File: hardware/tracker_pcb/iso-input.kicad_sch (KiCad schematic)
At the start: 5 parts, among them Q1 LTV-817S-TA1-D

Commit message: Including LORA wio-sx1262
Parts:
- D4: symbol ESP32-C6-EVB_Rev_A:D_Small -> Device:D_Filled; LCSC (none) -> C81598
- LED1: symbol ESP32-C6-EVB_Rev_A:LED -> Device:LED; LCSC (none) -> C2288
- Q1: LCSC (none) -> C114603
- R13: renamed from R11; LCSC (none) -> C22967
- renumbered R10 to R12
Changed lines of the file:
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@@
+	(wire
+		(pts
+			(xy 139.7 85.09) (xy 146.05 85.09)
+		)
+		(stroke
+			(width 0)
+			(type default)
+		)
+	)
 	(wire
 		(pts
@@
 	(wire
 		(pts
-			(xy 130.81 85.09) (xy 127 85.09)
-		)
-		(stroke
-			(width 0)
-			(type default)
-		)
-	)
-	(wire
-		(pts
 			(xy 173.99 90.17) (xy 173.99 97.79)
 		)
@@
 	(wire
 		(pts
-			(xy 140.97 85.09) (xy 146.05 85.09)
-		)
-		(stroke
-			(width 0)
-			(type default)
-		)
-	)
-	(wire
-		(pts
-			(xy 127 88.9) (xy 127 85.09)
+			(xy 127 85.09) (xy 132.08 85.09)
 		)
 		(stroke
@@
 	(wire
 		(pts
+			(xy 127 95.25) (xy 127 97.79)
+		)
+		(stroke
+			(width 0)
+			(type default)
+		)
+	)
+	(wire
+		(pts
 			(xy 127 97.79) (xy 146.05 97.79)
 		)
@@
 	(wire
 		(pts
-			(xy 127 93.98) (xy 127 97.79)
+			(xy 127 85.09) (xy 127 87.63)
 		)
 		(stroke
@@
 	)
 	(symbol
-		(lib_id "ESP32-C6-EVB_Rev_A:LED")
+		(lib_id "Device:LED")
 		(at 135.89 85.09 180)
 		(unit 1)
@@
 			(effects
 				(font
-					(size 1.524 1.524)
-				)
-				(hide yes)
-			)
-		)
-		(property "Datasheet" ""
+					(size 1.27 1.27)
+				)
+				(hide yes)
+			)
+		)
+		(property "Datasheet" "~"
 			(at 135.89 85.09 0)
 			(effects
 				(font
-					(size 1.524 1.524)
-				)
-			)
-		)
-		(property "Description" ""
+					(size 1.27 1.27)
+				)
+				(hide yes)
+			)
+		)
+		(property "Description" "Light emitting diode"
 			(at 135.89 85.09 0)
 			(effects
@@
 					(size 1.27 1.27)
 				)
+				(hide yes)
 			)
 		)
@@
 				(font
 					(size 1.524 1.524)
+				)
+				(hide yes)
+			)
+		)
+		(property "Sim.Pins" "1=K 2=A"
+			(at 135.89 85.09 0)
+			(effects
+				(font
+					(size 1.27 1.27)
+				)
+				(hide yes)
+			)
+		)
+		(property "LCSC" "C2288"
+			(at 133.35 82.55 0)
+			(effects
+				(font
+					(size 1.27 1.27)
 				)
 				(hide yes)
@@
 		(dnp no)
 		(fields_autoplaced yes)
-		(property "Reference" "R10"
+		(property "Reference" "R12"
 			(at 106.68 78.74 90)
 			(effects
@@
 			(project "tracker_pcb"
 				(path "/6aaa9514-f94e-4843-90d0-16960e4e49cb/04328898-976a-48a2-86bf-9938cb4aefd5"
+					(reference "R14")
+					(unit 1)
+				)
+				(path "/6aaa9514-f94e-4843-90d0-16960e4e49cb/45a2292e-2f51-4a4c-a627-74180fb6fdfe"
+					(reference "R18")
+					(unit 1)
+				)
+				(path "/6aaa9514-f94e-4843-90d0-16960e4e49cb/45c78875-26ba-4b22-bc82-79a51b704824"
 					(reference "R12")
 					(unit 1)
 				)
-				(path "/6aaa9514-f94e-4843-90d0-16960e4e49cb/45a2292e-2f51-4a4c-a627-74180fb6fdfe"
+				(path "/6aaa9514-f94e-4843-90d0-16960e4e49cb/b128d80c-4aa3-4c05-bd4f-543db8edd72e"
 					(reference "R16")
-					(unit 1)
-				)
-				(path "/6aaa9514-f94e-4843-90d0-16960e4e49cb/45c78875-26ba-4b22-bc82-79a51b704824"
-					(reference "R10")
-					(unit 1)
-				)
-				(path "/6aaa9514-f94e-4843-90d0-16960e4e49cb/b128d80c-4aa3-4c05-bd4f-543db8edd72e"
-					(reference "R14")
 					(unit 1)
 				)
@@
 		(on_board yes)
 		(dnp no)
-		(property "Reference" "#PWR015"
+		(property "Reference" "#PWR016"
 			(at 173.99 104.14 0)
 			(effects
@@
 			(project "tracker_pcb"
 				(path "/6aaa9514-f94e-4843-90d0-16960e4e49cb/04328898-976a-48a2-86bf-9938cb4aefd5"
+					(reference "#PWR017")
+					(unit 1)
+				)
+				(path "/6aaa9514-f94e-4843-90d0-16960e4e49cb/45a2292e-2f51-4a4c-a627-74180fb6fdfe"
+					(reference "#PWR019")
+					(unit 1)
+				)
+				(path "/6aaa9514-f94e-4843-90d0-16960e4e49cb/45c78875-26ba-4b22-bc82-79a51b704824"
 					(reference "#PWR016")
 					(unit 1)
 				)
-				(path "/6aaa9514-f94e-4843-90d0-16960e4e49cb/45a2292e-2f51-4a4c-a627-74180fb6fdfe"
+				(path "/6aaa9514-f94e-4843-90d0-16960e4e49cb/b128d80c-4aa3-4c05-bd4f-543db8edd72e"
 					(reference "#PWR018")
-					(unit 1)
-				)
-				(path "/6aaa9514-f94e-4843-90d0-16960e4e49cb/45c78875-26ba-4b22-bc82-79a51b704824"
-					(reference "#PWR015")
-					(unit 1)
-				)
-				(path "/6aaa9514-f94e-4843-90d0-16960e4e49cb/b128d80c-4aa3-4c05-bd4f-543db8edd72e"
-					(reference "#PWR017")
 					(unit 1)
 				)
@@
 		(dnp no)
 		(fields_autoplaced yes)
-		(property "Reference" "R11"
+		(property "Reference" "R13"
 			(at 181.61 73.6599 0)
 			(effects
@@
 		(property "Description" "Resistor, US symbol"
 			(at 179.07 74.93 0)
+			(effects
+				(font
+					(size 1.27 1.27)
+				)
+				(hide yes)
+			)
+		)
+		(property "LCSC" "C22967"
+			(at 181.61 73.6599 0)
 			(effects
 				(font
@@
 			(project "tracker_pcb"
 				(path "/6aaa9514-f94e-4843-90d0-16960e4e49cb/04328898-976a-48a2-86bf-9938cb4aefd5"
+					(reference "R15")
+					(unit 1)
+				)
+				(path "/6aaa9514-f94e-4843-90d0-16960e4e49cb/45a2292e-2f51-4a4c-a627-74180fb6fdfe"
+					(reference "R19")
+					(unit 1)
+				)
+				(path "/6aaa9514-f94e-4843-90d0-16960e4e49cb/45c78875-26ba-4b22-bc82-79a51b704824"
 					(reference "R13")
 					(unit 1)
 				)
-				(path "/6aaa9514-f94e-4843-90d0-16960e4e49cb/45a2292e-2f51-4a4c-a627-74180fb6fdfe"
+				(path "/6aaa9514-f94e-4843-90d0-16960e4e49cb/b128d80c-4aa3-4c05-bd4f-543db8edd72e"
 					(reference "R17")
-					(unit 1)
-				)
-				(path "/6aaa9514-f94e-4843-90d0-16960e4e49cb/45c78875-26ba-4b22-bc82-79a51b704824"
-					(reference "R11")
-					(unit 1)
-				)
-				(path "/6aaa9514-f94e-4843-90d0-16960e4e49cb/b128d80c-4aa3-4c05-bd4f-543db8edd72e"
-					(reference "R15")
 					(unit 1)
 				)
@@
 			)
 		)
+		(property "LCSC" "C114603"
+			(at 160.02 77.47 0)
+			(effects
+				(font
+					(size 1.27 1.27)
+				)
+				(hide yes)
+			)
+		)
 		(pin "3"
 		)
@@
 	)
 	(symbol
-		(lib_id "ESP32-C6-EVB_Rev_A:D_Small")
+		(lib_id "Device:D_Filled")
 		(at 127 91.44 90)
 		(mirror x)
@@
 		)
 		(property "Footprint" "Diode_SMD:D_SOD-123"
-			(at 124.7648 93.7514 90)
-			(effects
-				(font
-					(size 1.524 1.524)
-				)
-				(justify left)
-				(hide yes)
-			)
-		)
-		(property "Datasheet" ""
-			(at 127 91.44 90)
-			(effects
-				(font
-					(size 1.524 1.524)
-				)
-			)
-		)
-		(property "Description" ""
 			(at 127 91.44 0)
 			(effects
@@
 					(size 1.27 1.27)
 				)
-			)
-		)
+				(hide yes)
+			)
+		)
+		(property "Datasheet" "~"
+			(at 127 91.44 0)
+			(effects
+				(font
+					(size 1.27 1.27)
+				)
+				(hide yes)
+			)
+		)
+		(property "Description" "Diode, filled shape"
+			(at 127 91.44 0)
+			(effects
+				(font
+					(size 1.27 1.27)
+				)
+				(hide yes)
+			)
+		)
+		(property "Sim.Device" "D"
+			(at 127 91.44 0)
+			(effects
+				(font
+					(size 1.27 1.27)
+				)
+				(hide yes)
+			)
+		)
+		(property "Sim.Pins" "1=K 2=A"
+			(at 127 91.44 0)
+			(effects
+				(font
+					(size 1.27 1.27)
+				)
+				(hide yes)
+			)
+		)
+		(property "LCSC" "C81598"
+			(at 125.73 86.36 0)
+			(effects
+				(font
+					(size 1.27 1.27)
+				)
+				(hide yes)
+			)
+		)

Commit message: VIA changes
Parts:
- R12: LCSC (none) -> C17513
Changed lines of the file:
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@@
+			)
+		)
+		(property "LCSC" "C17513"
+			(at 106.68 78.74 0)
+			(effects
+				(font
+					(size 1.27 1.27)
+				)
+				(hide yes)
 			)
 		)

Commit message: Beef up 5v supply and add new power mux
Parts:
- D4: footprint Diode_SMD:D_SOD-123 -> Diode_SMD:D_SOD-323; symbol Device:D_Filled -> Diode:1N4148WS
- renumbered R12 to R11, R13 to R12
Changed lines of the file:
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@@
 		(dnp no)
 		(fields_autoplaced yes)
-		(property "Reference" "R12"
+		(property "Reference" "R11"
 			(at 106.68 78.74 90)
 			(effects
@@
 			(project "tracker_pcb"
 				(path "/6aaa9514-f94e-4843-90d0-16960e4e49cb/04328898-976a-48a2-86bf-9938cb4aefd5"
-					(reference "R14")
+					(reference "R13")
 					(unit 1)
 				)
 				(path "/6aaa9514-f94e-4843-90d0-16960e4e49cb/45a2292e-2f51-4a4c-a627-74180fb6fdfe"
-					(reference "R18")
+					(reference "R17")
 					(unit 1)
 				)
 				(path "/6aaa9514-f94e-4843-90d0-16960e4e49cb/45c78875-26ba-4b22-bc82-79a51b704824"
-					(reference "R12")
+					(reference "R11")
 					(unit 1)
 				)
 				(path "/6aaa9514-f94e-4843-90d0-16960e4e49cb/b128d80c-4aa3-4c05-bd4f-543db8edd72e"
-					(reference "R16")
+					(reference "R15")
 					(unit 1)
 				)
@@
 		(on_board yes)
 		(dnp no)
-		(property "Reference" "#PWR016"
+		(property "Reference" "#PWR018"
 			(at 173.99 104.14 0)
 			(effects
@@
 			(project "tracker_pcb"
 				(path "/6aaa9514-f94e-4843-90d0-16960e4e49cb/04328898-976a-48a2-86bf-9938cb4aefd5"
-					(reference "#PWR017")
+					(reference "#PWR019")
 					(unit 1)
 				)
 				(path "/6aaa9514-f94e-4843-90d0-16960e4e49cb/45a2292e-2f51-4a4c-a627-74180fb6fdfe"
-					(reference "#PWR019")
+					(reference "#PWR021")
 					(unit 1)
 				)
 				(path "/6aaa9514-f94e-4843-90d0-16960e4e49cb/45c78875-26ba-4b22-bc82-79a51b704824"
-					(reference "#PWR016")
+					(reference "#PWR018")
 					(unit 1)
 				)
 				(path "/6aaa9514-f94e-4843-90d0-16960e4e49cb/b128d80c-4aa3-4c05-bd4f-543db8edd72e"
-					(reference "#PWR018")
+					(reference "#PWR020")
 					(unit 1)
 				)
@@
 		(dnp no)
 		(fields_autoplaced yes)
-		(property "Reference" "R13"
+		(property "Reference" "R12"
 			(at 181.61 73.6599 0)
 			(effects
@@
 			(project "tracker_pcb"
 				(path "/6aaa9514-f94e-4843-90d0-16960e4e49cb/04328898-976a-48a2-86bf-9938cb4aefd5"
-					(reference "R15")
+					(reference "R14")
 					(unit 1)
 				)
 				(path "/6aaa9514-f94e-4843-90d0-16960e4e49cb/45a2292e-2f51-4a4c-a627-74180fb6fdfe"
-					(reference "R19")
+					(reference "R18")
 					(unit 1)
 				)
 				(path "/6aaa9514-f94e-4843-90d0-16960e4e49cb/45c78875-26ba-4b22-bc82-79a51b704824"
-					(reference "R13")
+					(reference "R12")
 					(unit 1)
 				)
 				(path "/6aaa9514-f94e-4843-90d0-16960e4e49cb/b128d80c-4aa3-4c05-bd4f-543db8edd72e"
-					(reference "R17")
+					(reference "R16")
 					(unit 1)
 				)
@@
 	)
 	(symbol
-		(lib_id "Device:D_Filled")
+		(lib_id "Diode:1N4148WS")
 		(at 127 91.44 90)
 		(mirror x)
@@
 			)
 		)
-		(property "Footprint" "Diode_SMD:D_SOD-123"
+		(property "Footprint" "Diode_SMD:D_SOD-323"
+			(at 131.445 91.44 0)
+			(effects
+				(font
+					(size 1.27 1.27)
+				)
+				(hide yes)
+			)
+		)
+		(property "Datasheet" "https://www.vishay.com/docs/85751/1n4148ws.pdf"
 			(at 127 91.44 0)
 			(effects
@@
 			)
 		)
-		(property "Datasheet" "~"
+		(property "Description" "75V 0.15A Fast switching Diode, SOD-323"
 			(at 127 91.44 0)
 			(effects
-				(font
-					(size 1.27 1.27)
-				)
-				(hide yes)
-			)
-		)
-		(property "Description" "Diode, filled shape"
-			(at 127 91.44 0)
-			(effects

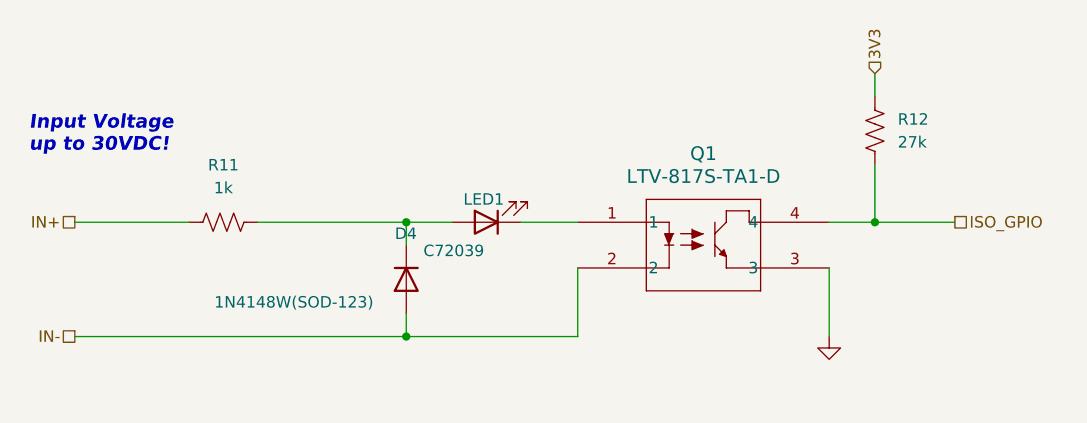
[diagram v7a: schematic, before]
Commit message: Modify iso circuit for best CTR
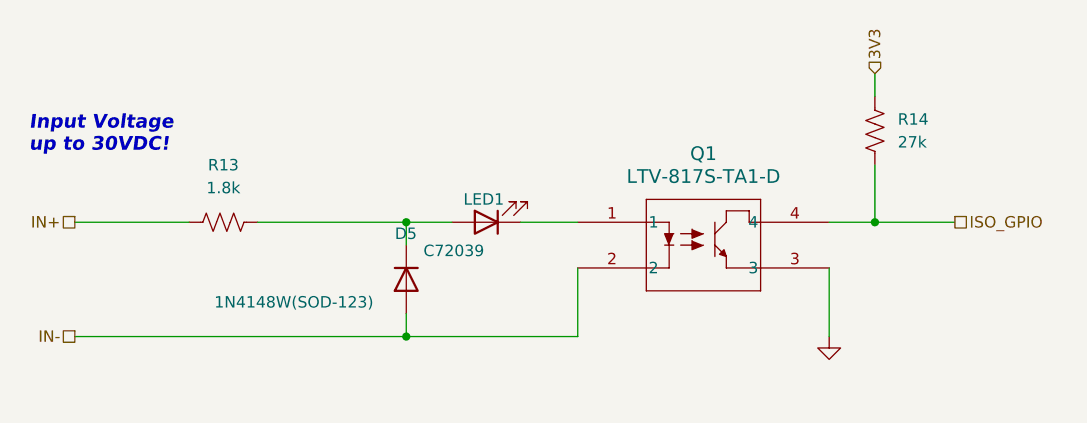
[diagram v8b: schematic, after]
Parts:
- R13: renamed from R11; value 1k -> 1.8k
- renumbered D4 to D5, R12 to R14
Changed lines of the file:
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@@
 		(dnp no)
 		(fields_autoplaced yes)
-		(property "Reference" "R11"
+		(property "Reference" "R13"
 			(at 106.68 78.74 90)
 			(effects
@@
 			)
 		)
-		(property "Value" "1k"
+		(property "Value" "1.8k"
 			(at 106.68 81.28 90)
 			(effects
@@
 			(project "tracker_pcb"
 				(path "/6aaa9514-f94e-4843-90d0-16960e4e49cb/04328898-976a-48a2-86bf-9938cb4aefd5"
+					(reference "R15")
+					(unit 1)
+				)
+				(path "/6aaa9514-f94e-4843-90d0-16960e4e49cb/45a2292e-2f51-4a4c-a627-74180fb6fdfe"
+					(reference "R19")
+					(unit 1)
+				)
+				(path "/6aaa9514-f94e-4843-90d0-16960e4e49cb/45c78875-26ba-4b22-bc82-79a51b704824"
 					(reference "R13")
 					(unit 1)
 				)
-				(path "/6aaa9514-f94e-4843-90d0-16960e4e49cb/45a2292e-2f51-4a4c-a627-74180fb6fdfe"
+				(path "/6aaa9514-f94e-4843-90d0-16960e4e49cb/b128d80c-4aa3-4c05-bd4f-543db8edd72e"
 					(reference "R17")
-					(unit 1)
-				)
-				(path "/6aaa9514-f94e-4843-90d0-16960e4e49cb/45c78875-26ba-4b22-bc82-79a51b704824"
-					(reference "R11")
-					(unit 1)
-				)
-				(path "/6aaa9514-f94e-4843-90d0-16960e4e49cb/b128d80c-4aa3-4c05-bd4f-543db8edd72e"
-					(reference "R15")
 					(unit 1)
 				)
@@
 		(dnp no)
 		(fields_autoplaced yes)
-		(property "Reference" "R12"
+		(property "Reference" "R14"
 			(at 181.61 73.6599 0)
 			(effects
@@
 			(project "tracker_pcb"
 				(path "/6aaa9514-f94e-4843-90d0-16960e4e49cb/04328898-976a-48a2-86bf-9938cb4aefd5"
+					(reference "R16")
+					(unit 1)
+				)
+				(path "/6aaa9514-f94e-4843-90d0-16960e4e49cb/45a2292e-2f51-4a4c-a627-74180fb6fdfe"
+					(reference "R20")
+					(unit 1)
+				)
+				(path "/6aaa9514-f94e-4843-90d0-16960e4e49cb/45c78875-26ba-4b22-bc82-79a51b704824"
 					(reference "R14")
 					(unit 1)
 				)
-				(path "/6aaa9514-f94e-4843-90d0-16960e4e49cb/45a2292e-2f51-4a4c-a627-74180fb6fdfe"
+				(path "/6aaa9514-f94e-4843-90d0-16960e4e49cb/b128d80c-4aa3-4c05-bd4f-543db8edd72e"
 					(reference "R18")
-					(unit 1)
-				)
-				(path "/6aaa9514-f94e-4843-90d0-16960e4e49cb/45c78875-26ba-4b22-bc82-79a51b704824"
-					(reference "R12")
-					(unit 1)
-				)
-				(path "/6aaa9514-f94e-4843-90d0-16960e4e49cb/b128d80c-4aa3-4c05-bd4f-543db8edd72e"
-					(reference "R16")
 					(unit 1)
 				)
@@
 		(on_board yes)
 		(dnp no)
-		(property "Reference" "D4"
+		(property "Reference" "D5"
 			(at 125.73 86.36 90)
 			(effects
@@
 			(project "tracker_pcb"
 				(path "/6aaa9514-f94e-4843-90d0-16960e4e49cb/04328898-976a-48a2-86bf-9938cb4aefd5"
+					(reference "D6")
+					(unit 1)
+				)
+				(path "/6aaa9514-f94e-4843-90d0-16960e4e49cb/45a2292e-2f51-4a4c-a627-74180fb6fdfe"
+					(reference "D8")
+					(unit 1)
+				)
+				(path "/6aaa9514-f94e-4843-90d0-16960e4e49cb/45c78875-26ba-4b22-bc82-79a51b704824"
 					(reference "D5")
 					(unit 1)
 				)
-				(path "/6aaa9514-f94e-4843-90d0-16960e4e49cb/45a2292e-2f51-4a4c-a627-74180fb6fdfe"
+				(path "/6aaa9514-f94e-4843-90d0-16960e4e49cb/b128d80c-4aa3-4c05-bd4f-543db8edd72e"
 					(reference "D7")
 					(unit 1)
 				)
-				(path "/6aaa9514-f94e-4843-90d0-16960e4e49cb/45c78875-26ba-4b22-bc82-79a51b704824"
-					(reference "D4")
-					(unit 1)
-				)
-				(path "/6aaa9514-f94e-4843-90d0-16960e4e49cb/b128d80c-4aa3-4c05-bd4f-543db8edd72e"
-					(reference "D6")
-					(unit 1)
-				)
